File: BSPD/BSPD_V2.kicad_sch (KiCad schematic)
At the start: 35 parts, among them J2 Conn_01x02_Socket, J3 Conn_01x02_Socket, J4 Conn_01x02_Socket, K1 Fujitsu_FTR-LYCA005x, Q1 AO3400A, Q2 AO3400A, Q3 NPN, Q4 AO3400A, Q5 NPN, U1 CD4001BM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

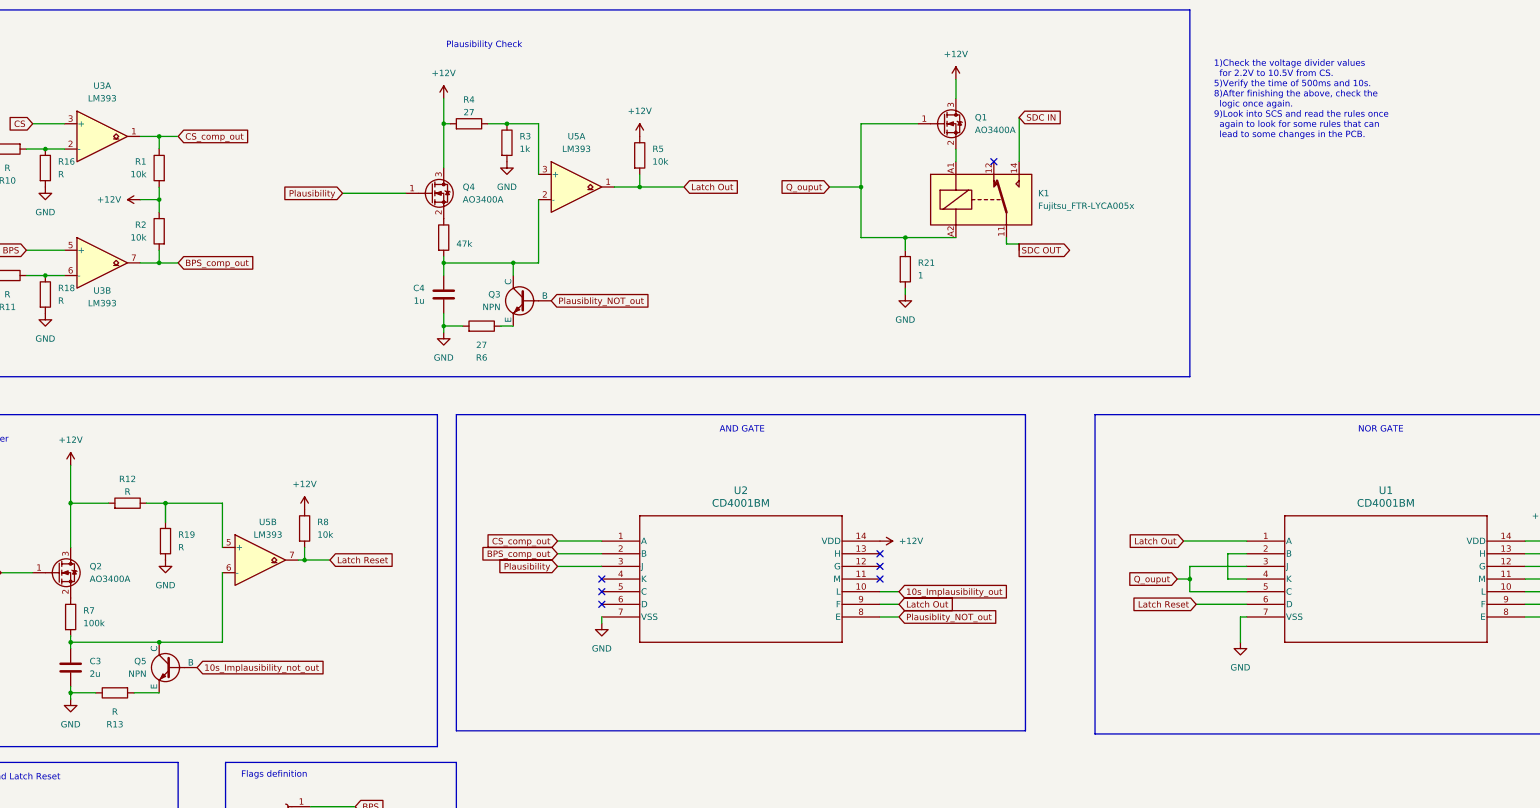
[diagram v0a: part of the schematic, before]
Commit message: Did the values for 10s Implausibility, have to verify whether using 10uF and 100k resistor is feasible
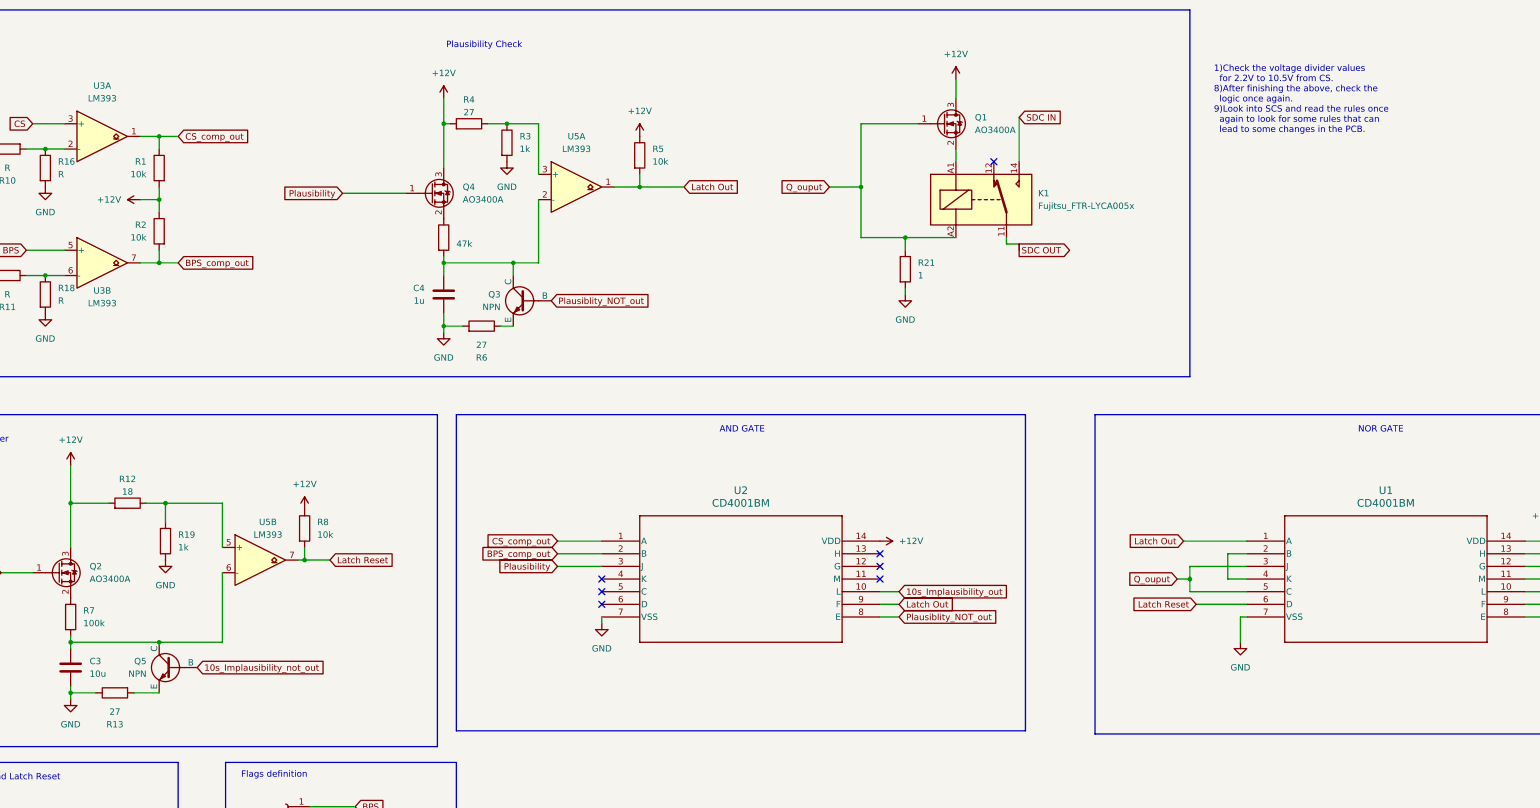
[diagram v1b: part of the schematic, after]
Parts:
- C3: value 2u -> 10u
- R12: value R -> 18
- R13: value R -> 27
- R19: value R -> 1k
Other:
- note added: "1)Check the voltage divider values for 2.2V to 10.5V from CS. 8)After finishing the above, check the logic once again. 9)Look into SCS and read the rules once again to look for some rules that can lead to some changes in the PCB."
- note removed: "1)Check the voltage divider values for 2.2V to 10.5V from CS. 5)Verify the time of 500ms and 10s. 8)After finishing the above, check the logic once again. 9)Look into SCS and read the rules once again to look for some rules that can lead to some changes in the PCB."
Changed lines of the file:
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@@
 		)
 	)
-	(text "1)Check the voltage divider values \n  for 2.2V to 10.5V from CS.\n5)Verify the time of 500ms and 10s. \n8)After finishing the above, check the\n  logic once again.\n9)Look into SCS and read the rules once\n  again to look for some rules that can\n  lead to some changes in the PCB.\n"
+	(text "1)Check the voltage divider values \n  for 2.2V to 10.5V from CS.\n8)After finishing the above, check the\n  logic once again.\n9)Look into SCS and read the rules once\n  again to look for some rules that can\n  lead to some changes in the PCB.\n"
 		(exclude_from_sim no)
 		(at 302.006 51.054 0)
@@
 			)
 		)
-		(property "Value" "2u"
+		(property "Value" "10u"
 			(at 76.2 166.3699 0)
 			(effects
@@
 			)
 		)
-		(property "Value" "R"
+		(property "Value" "1k"
 			(at 93.98 140.9699 0)
 			(effects
@@
 			)
 		)
-		(property "Value" "R"
+		(property "Value" "27"
 			(at 81.28 173.99 90)
 			(effects
@@
 			)
 		)
-		(property "Value" "R"
+		(property "Value" "18"
 			(at 83.82 129.794 90)
 			(effects

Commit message: Added all the rest of the resistor values Hopefully the logic is fine
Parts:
- added R15: 1, symbol Device:R
- R10: value R -> 1.8k
- R16: value R -> 1k
- R4: value 27 -> 24
- R9: value R -> 10k
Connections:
- net at R3.1, U5.3 (+): now also R15.2; no longer R4.1
- new net: R15.1, R4.1
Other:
- note added: "8)After finishing the above, check the logic once again. 9)Look into SCS and read the rules once again to look for some rules that can lead to some changes in the PCB."
- note removed: "1)Check the voltage divider values for 2.2V to 10.5V from CS. 8)After finishing the above, check the logic once again. 9)Look into SCS and read the rules once again to look for some rules that can lead to some changes in the PCB."
- moved on the sheet: C3, C4, K1, Q1, Q2, Q3, Q4, Q5, R1, R10, R11, R12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
